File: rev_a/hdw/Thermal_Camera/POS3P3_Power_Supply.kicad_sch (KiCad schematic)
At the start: 0 parts

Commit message: copied lots of circuitry to reuse
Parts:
- added C? (x2): 0.1uF, Capacitors_SMD:C_0603, symbol Custom_Library:C_Custom
- added C?: 10uF, Capacitors_SMD:C_0603, symbol Custom_Library:C_Custom
- added C? (x4): 10uF, Capacitors_SMD:C_1206, symbol Custom_Library:C_Custom
- added C?: 10nF, Capacitors_SMD:C_0603, symbol Custom_Library:C_Custom
- added D?: BAT48JFILM, Diode_SMD:D_SOD-323, symbol Diode:BAT48JFILM
- added L?: 2.2uH, Inductors_SMD:L_Vishay_IHLP-2020, symbol Custom_Library:L_Custom
- added Q?: BSS214NW, Package_TO_SOT_SMD:SOT-323_SC-70, symbol Transistor_FET:BSS214NW
- added Q?: ZXMS6004FFTA, Package_TO_SOT_SMD:SOT-23, symbol Custom_Library:ZXMS6004FFTA
- added R?: 1.37k, Resistors_SMD:R_0603, symbol Custom_Library:R_Custom
- added R?: 180k, Resistors_SMD:R_0603, symbol Custom_Library:R_Custom
- added R? (x2): 10, Resistors_SMD:R_0603, symbol Custom_Library:R_Custom
- added R?: 953k, Resistors_SMD:R_0603, symbol Custom_Library:R_Custom
- added R? (x2): 10k, Resistors_SMD:R_0603, symbol Custom_Library:R_Custom
- added R?: 2.67k, Resistors_SMD:R_0603, symbol Custom_Library:R_Custom
- added TP?: TP, Custom Footprints Library:Test_Point, symbol Custom_Library:TP
- added U?: 74LVC1G97, Package_TO_SOT_SMD:SOT-363_SC-70-6, symbol Custom_Library:74LVC1G97_Power_AND
- added U?: TPS62133, Package_DFN_QFN:QFN-16-1EP_3x3mm_P0.5mm_EP1.75x1.75mm, symbol Custom_Library:TPS62130
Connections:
- new net: C?.1, D?.1 (K), R?.1
- new net: R?.2, U?.4
- new net: R?.1, R?.1, R?.2, U?.5 (FB)
- new net: R?.2, U?.4 (PG), U?.6
- new net: Q?.1 (G), Q?.3 (D), R?.2
- new net: L?.1, U?.1 (SW), U?.2 (SW), U?.3 (SW)
- new net: C?.1, U?.9 (SS/TR)
- new net +12V: C?.1, C?.1, C?.1, U?.10 (AVIN), U?.11 (PVIN), U?.12 (PVIN)
- new net +5VP: C?.1, C?.1, C?.1, D?.2 (A), L?.2, Q?.3 (D), R?.1, R?.1, TP?.1 (TP), U?.14 (VOS), U?.5 (VCC)
- new net GND: C?.2, C?.2, C?.2, C?.2, C?.2, C?.2, C?.2, C?.2, Q?.2 (S), Q?.2 (S), R?.2, R?.2, R?.2, U?.1 (GND), U?.15 (PGND), U?.16 (PGND), U?.17 (EP), U?.2 (GND), U?.6 (AGND), U?.7 (FSW), U?.8 (DEF)
- new net POS12_PGOOD: R?.1
- new net POS5P_PGOOD: R?.1, R?.1
- new net POS5P_RUN: Q?.1 (G), R?.2, U?.13 (EN), U?.3
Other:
- note added: "CHANGE TO +3.3V"
- note added: "Fixed VOUT = +5V"

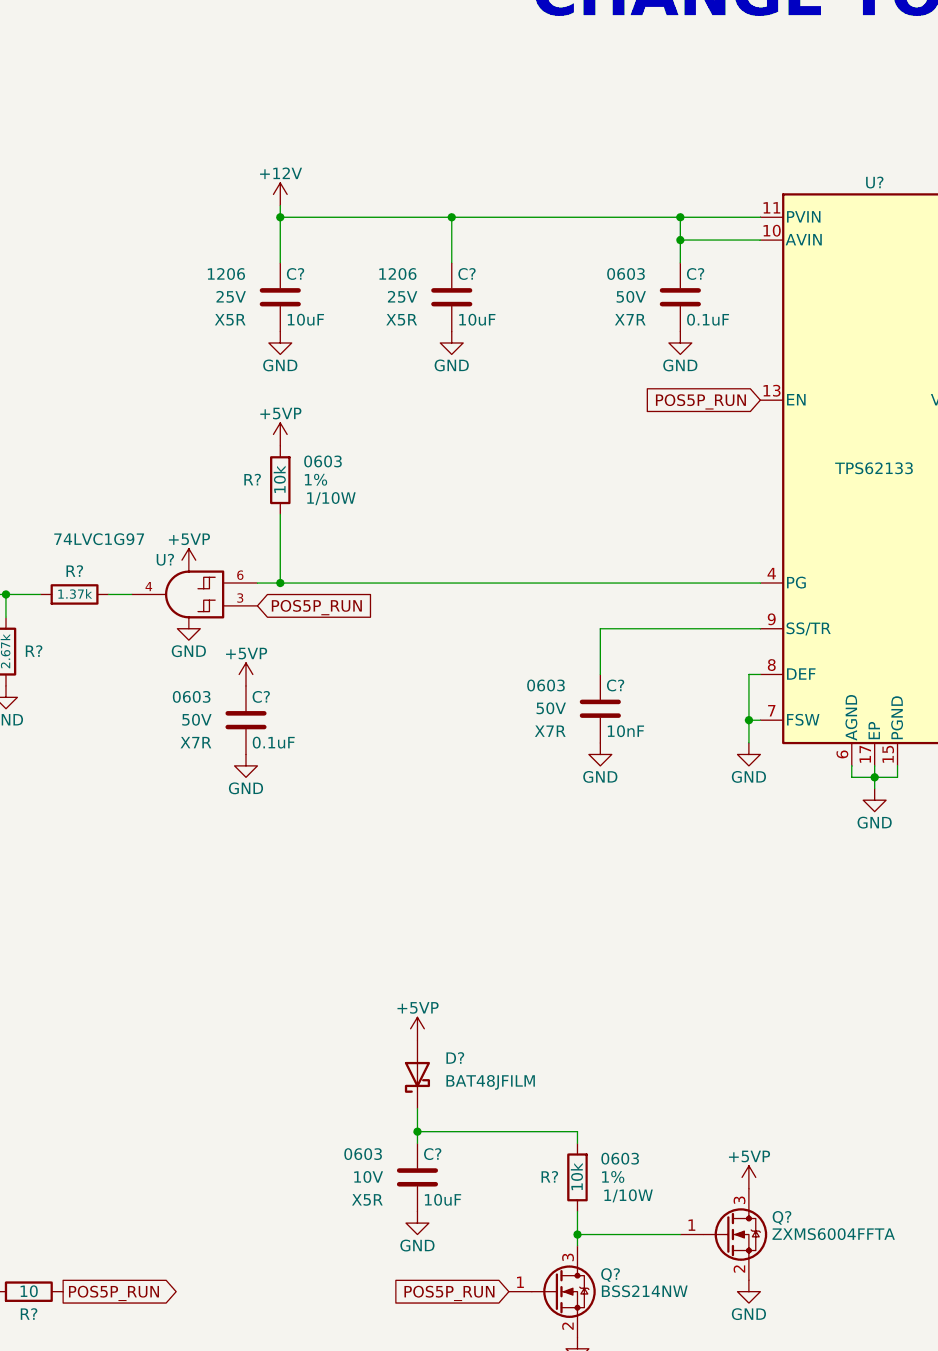
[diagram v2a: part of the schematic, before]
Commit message: added many more blank schematic sheets
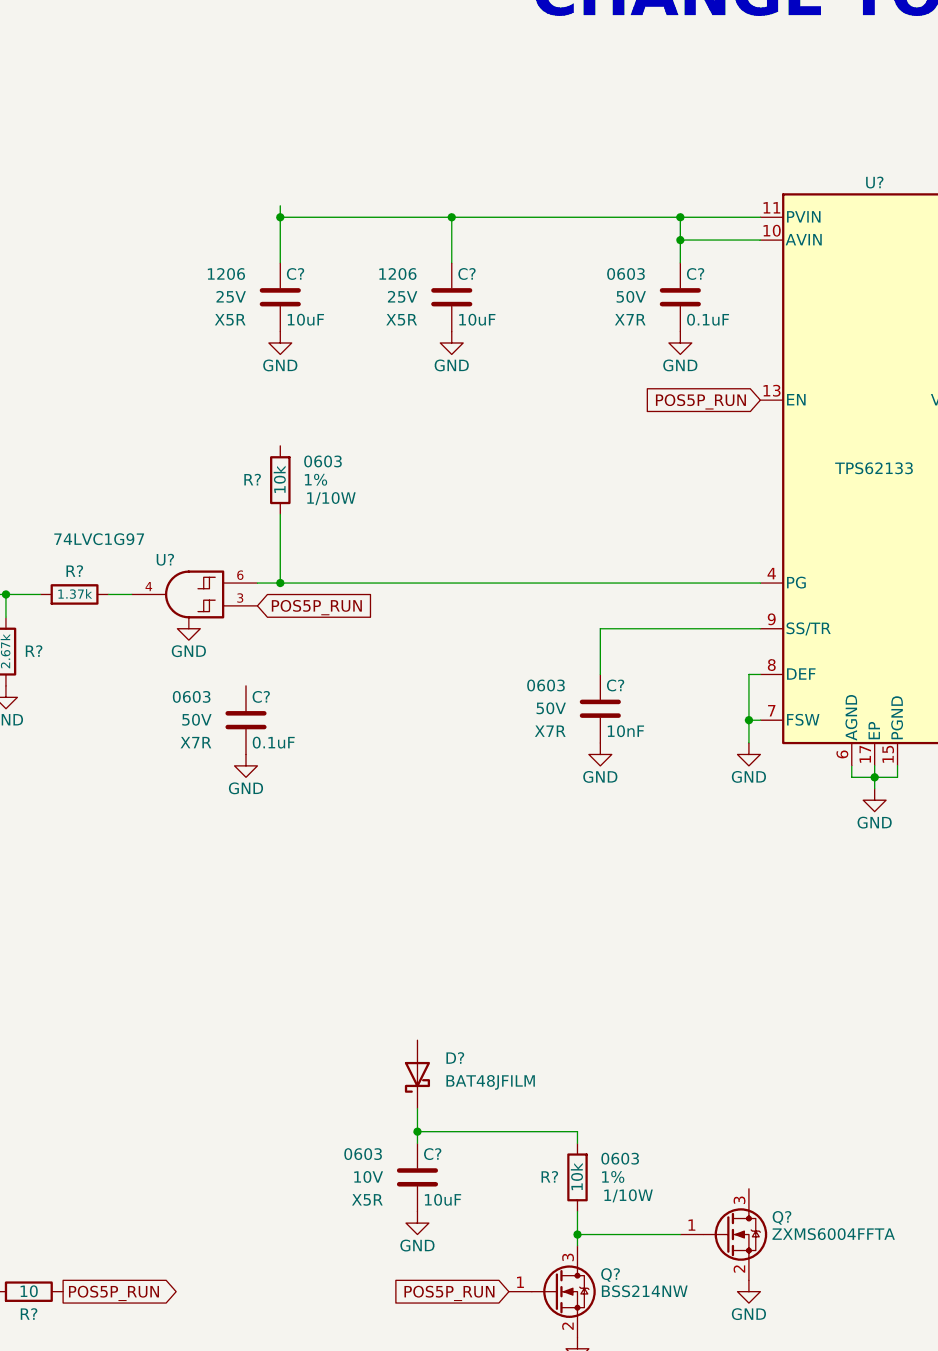
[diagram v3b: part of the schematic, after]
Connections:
- net +5VP: no longer C?.1, D?.2 (A), Q?.3 (D), R?.1, U?.5 (VCC)
- net +12V: no longer names the net of C?.1, C?.1, C?.1, U?.10 (AVIN), U?.11 (PVIN), U?.12 (PVIN)
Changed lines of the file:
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@@
   (title_block
     (title "Thermal Camera")
-    (date "2023-11-12")
+    (date "2023-11-13")
     (rev "PRELIM")
     (company "Drew Maatman and Michael Laffin")
@@
         (path "/e85aac8c-404c-45dd-bda3-1057cae83baf/00000000-0000-0000-0000-00005f41a7c7"
           (reference "#PWR0313") (unit 1)
-        )
-      )
-    )
-  )
-  (symbol (lib_id "power:+12V") (at 73.66 48.26 0) (unit 1)
-    (in_bom yes) (on_board yes) (dnp no)
-    (property "Reference" "#PWR0406" (at 73.66 52.07 0)
-      (effects (font (size 1.27 1.27)) hide)
-    )
-    (property "Value" "+12V" (at 73.66 44.704 0)
-      (effects (font (size 1.27 1.27)))
-    )
-    (property "Footprint" "" (at 73.66 48.26 0)
-      (effects (font (size 1.27 1.27)) hide)
-    )
-    (property "Datasheet" "" (at 73.66 48.26 0)
-      (effects (font (size 1.27 1.27)) hide)
-    )
-    (pin "1")
-    (instances
-      (project "Thermal_Camera"
-        (path "/4bd21e0b-5408-4b93-866e-c82ac5b31fa9/3996b81d-92d5-40b5-9537-6a34278c1c5b"
-          (reference "#PWR0406") (unit 1)
-        )
-      )
-      (project "LED_Panel_Controller"
-        (path "/9a153a92-537f-48f9-b716-589877e287a5/00000000-0000-0000-0000-00005e0dc082"
-          (reference "#PWR?") (unit 1)
-        )
-        (path "/9a153a92-537f-48f9-b716-589877e287a5/00000000-0000-0000-0000-00005eae2d8a"
-          (reference "#PWR?") (unit 1)
-        )
-        (path "/9a153a92-537f-48f9-b716-589877e287a5/00000000-0000-0000-0000-00005cb7718d"
-          (reference "#PWR?") (unit 1)
-        )
-        (path "/9a153a92-537f-48f9-b716-589877e287a5/00000000-0000-0000-0000-00005f581ba3"
-          (reference "#PWR?") (unit 1)
-        )
-        (path "/9a153a92-537f-48f9-b716-589877e287a5/00000000-0000-0000-0000-00005e0f263a"
-          (reference "#PWR?") (unit 1)
-        )
-      )
-      (project "USB_Hub"
-        (path "/e85aac8c-404c-45dd-bda3-1057cae83baf/00000000-0000-0000-0000-00005f41a7c7"
-          (reference "#PWR0306") (unit 1)
         )
       )
@@
     )
   )
-  (symbol (lib_id "power:+5VP") (at 69.85 101.6 0) (unit 1)
-    (in_bom yes) (on_board yes) (dnp no)
-    (property "Reference" "#PWR0404" (at 69.85 105.41 0)
-      (effects (font (size 1.27 1.27)) hide)
-    )
-    (property "Value" "+5VP" (at 69.85 98.044 0)
-      (effects (font (size 1.27 1.27)))
-    )
-    (property "Footprint" "" (at 69.85 101.6 0)
-      (effects (font (size 1.27 1.27)) hide)
-    )
-    (property "Datasheet" "" (at 69.85 101.6 0)
-      (effects (font (size 1.27 1.27)) hide)
-    )
-    (pin "1")
-    (instances
-      (project "Thermal_Camera"
-        (path "/4bd21e0b-5408-4b93-866e-c82ac5b31fa9/3996b81d-92d5-40b5-9537-6a34278c1c5b"
-          (reference "#PWR0404") (unit 1)
-        )
-      )
-      (project "USB_Hub"
-        (path "/e85aac8c-404c-45dd-bda3-1057cae83baf/00000000-0000-0000-0000-00005f41a7c7"
-          (reference "#PWR0304") (unit 1)
-        )
-      )
-    )
-  )
   (symbol (lib_id "power:GND") (at 106.68 173.99 0) (unit 1)
     (in_bom yes) (on_board yes) (dnp no)
@@
     )
   )
-  (symbol (lib_id "power:+5VP") (at 125.73 157.48 0) (unit 1)
-    (in_bom yes) (on_board yes) (dnp no)
-    (property "Reference" "#PWR0416" (at 125.73 161.29 0)
-      (effects (font (size 1.27 1.27)) hide)
-    )
-    (property "Value" "+5VP" (at 125.73 153.924 0)
-      (effects (font (size 1.27 1.27)))
-    )
-    (property "Footprint" "" (at 125.73 157.48 0)
-      (effects (font (size 1.27 1.27)) hide)
-    )
-    (property "Datasheet" "" (at 125.73 157.48 0)
-      (effects (font (size 1.27 1.27)) hide)
-    )
-    (pin "1")
-    (instances
-      (project "Thermal_Camera"
-        (path "/4bd21e0b-5408-4b93-866e-c82ac5b31fa9/3996b81d-92d5-40b5-9537-6a34278c1c5b"
-          (reference "#PWR0416") (unit 1)
-        )
-      )
-      (project "USB_Hub"
-        (path "/e85aac8c-404c-45dd-bda3-1057cae83baf/00000000-0000-0000-0000-00005f41a7c7"
-          (reference "#PWR0315") (unit 1)
-        )
-      )
-    )
-  )
   (symbol (lib_id "Custom_Library:L_Custom") (at 163.83 59.69 90) (unit 1)
     (in_bom yes) (on_board yes) (dnp no)
@@
     )
   )
-  (symbol (lib_id "power:+5VP") (at 88.9 140.97 0) (unit 1)
-    (in_bom yes) (on_board yes) (dnp no)
-    (property "Reference" "#PWR0409" (at 88.9 144.78 0)
-      (effects (font (size 1.27 1.27)) hide)
-    )
-    (property "Value" "+5VP" (at 88.9 137.414 0)
-      (effects (font (size 1.27 1.27)))
-    )
-    (property "Footprint" "" (at 88.9 140.97 0)
-      (effects (font (size 1.27 1.27)) hide)
-    )
-    (property "Datasheet" "" (at 88.9 140.97 0)
-      (effects (font (size 1.27 1.27)) hide)
-    )
-    (pin "1")
-    (instances
-      (project "Thermal_Camera"
-        (path "/4bd21e0b-5408-4b93-866e-c82ac5b31fa9/3996b81d-92d5-40b5-9537-6a34278c1c5b"
-          (reference "#PWR0409") (unit 1)
-        )
-      )
-      (project "USB_Hub"
-        (path "/e85aac8c-404c-45dd-bda3-1057cae83baf/00000000-0000-0000-0000-00005f41a7c7"
-          (reference "#PWR0309") (unit 1)
-        )
-      )
-    )
-  )
   (symbol (lib_id "Custom_Library:C_Custom") (at 92.71 58.42 0) (unit 1)
     (in_bom yes) (on_board yes) (dnp no)
@@
     )
   )
-  (symbol (lib_id "power:+5VP") (at 73.66 74.93 0) (unit 1)
-    (in_bom yes) (on_board yes) (dnp no)
-    (property "Reference" "#PWR0408" (at 73.66 78.74 0)
-      (effects (font (size 1.27 1.27)) hide)
-    )
-    (property "Value" "+5VP" (at 73.66 71.374 0)
-      (effects (font (size 1.27 1.27)))
-    )
-    (property "Footprint" "" (at 73.66 74.93 0)
-      (effects (font (size 1.27 1.27)) hide)
-    )
-    (property "Datasheet" "" (at 73.66 74.93 0)
-      (effects (font (size 1.27 1.27)) hide)
-    )
-    (pin "1")
-    (instances
-      (project "Thermal_Camera"
-        (path "/4bd21e0b-5408-4b93-866e-c82ac5b31fa9/3996b81d-92d5-40b5-9537-6a34278c1c5b"
-          (reference "#PWR0408") (unit 1)
-        )
-      )
-      (project "USB_Hub"
-        (path "/e85aac8c-404c-45dd-bda3-1057cae83baf/00000000-0000-0000-0000-00005f41a7c7"
-          (reference "#PWR0308") (unit 1)
-        )
-      )
-    )
-  )
   (symbol (lib_id "power:GND") (at 139.7 113.03 0) (unit 1)
     (in_bom yes) (on_board yes) (dnp no)
@@
         )
       )
-    )
-  )
-  (symbol (lib_id "power:+5VP") (at 63.5 88.9 0) (unit 1)
-    (in_bom yes) (on_board yes) (dnp no)
-    (property "Reference" "#PWR0402" (at 63.5 92.71 0)
-      (effects (font (size 1.27 1.27)) hide)
-    )
-    (property "Value" "+5VP" (at 63.5 85.344 0)
-      (effects (font (size 1.27 1.27)))
-    )
-    (property "Footprint" "" (at 63.5 88.9 0)
-      (effects (font (size 1.27 1.27)) hide)
-    )
-    (property "Datasheet" "" (at 63.5 88.9 0)
-      (effects (font (size 1.27 1.27)) hide)
-    )
-    (pin "1")
-    (instances
-      (project "Thermal_Camera"
-        (path "/4bd21e0b-5408-4b93-866e-c82ac5b31fa9/3996b81d-92d5-40b5-9537-6a34278c1c5b"
-          (reference "#PWR0402") (unit 1)
-        )
-      )
-      (project "USB_Hub"
-        (path "/e85aac8c-404c-45dd-bda3-1057cae83baf/00000000-0000-0000-0000-00005f41a7c7"
-          (reference "#PWR0302") (unit 1)
-        )
-      )

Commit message: added some power supplies
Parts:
- removed R?: 1.37k, Resistors_SMD:R_0603, symbol Custom_Library:R_Custom
- removed R?: 10, Resistors_SMD:R_0603, symbol Custom_Library:R_Custom
- removed R?: 2.67k, Resistors_SMD:R_0603, symbol Custom_Library:R_Custom
- added R?: 10k, Resistors_SMD:R_0603, symbol Custom_Library:R_Custom
- R?: value 180k -> 1.15k; Configuration DNP -> (none); Digi-Key PN 541-180KHCT-ND -> (none)
- R?: value 953k -> 3.57k; Configuration DNP -> (none); Digi-Key PN 541-953KHCT-ND -> (none)
- U?: value TPS62133 -> TPS62130A; Digi-Key PN 296-30225-1-ND -> 296-39446-1-ND
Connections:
- net +5VP is gone; now on net +3.3V: C?.1, C?.1, L?.2, R?.1, TP?.1 (TP), U?.14 (VOS)
- net GND: now also R?.2
- net +3.3V: now reaches C?.1
- net +3.3V: now also D?.2 (A), Q?.3 (D), R?.1, U?.5 (VCC)
- net POS3P3_PGOOD: now reaches U?.4
- net POS3P3_PGOOD: now also R?.1
- net VBAT: now reaches C?.1, C?.1, C?.1, U?.10 (AVIN), U?.11 (PVIN), U?.12 (PVIN)
- net POS5P_RUN renamed POS3P3_RUN
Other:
- note added: "figure out sequencing switch to +3.0V?"
- note removed: "CHANGE TO +3.3V"
- note removed: "Fixed VOUT = +5V"
